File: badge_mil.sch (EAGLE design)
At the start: 29 parts, among them U1 TINY2313-*S*, X1 FH12-10S-0.5SH

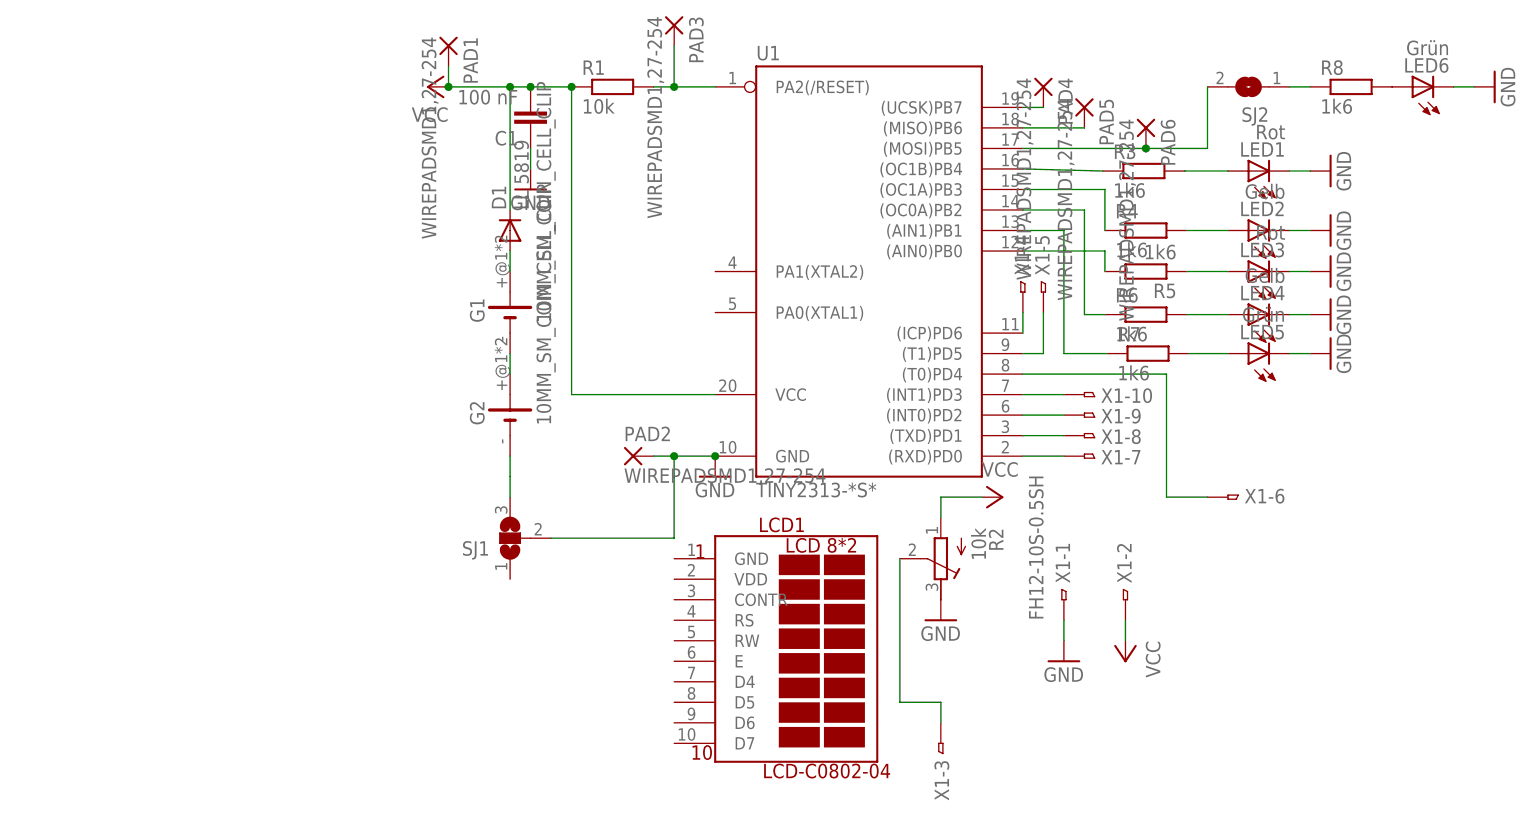
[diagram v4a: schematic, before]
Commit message: redesign, add render scripts
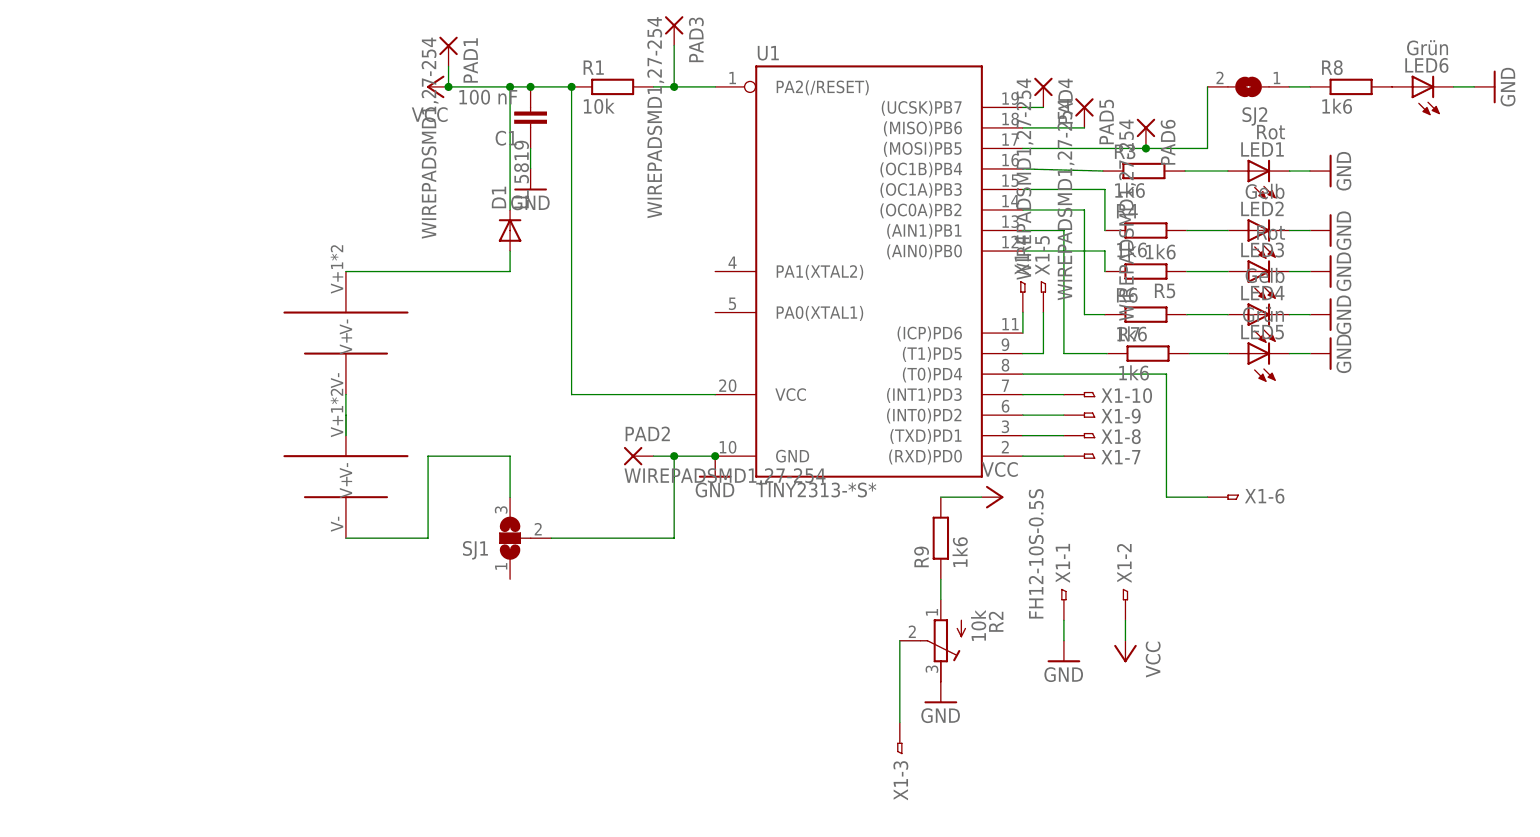
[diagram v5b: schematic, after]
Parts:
- removed G1, G2: 10MM_SM_COIN_CELL_CLIP, battery:10MM_SM_COIN_CELL_CLIP
- removed LCD1: LCD-C0802-04, lcd-c0802-04:LCD-C0802-04
- added R9: 1k6, resistor:R-EU_R0805
- added U$1, U$2: KEYSTONE3002, draradech:KEYSTONE3002
- X1: value FH12-10S-0.5SH -> FH12-10S-0.5S; device con-hirose:FH12-10S-0.5SH -> con-hirose:FH12-10S-0.5S
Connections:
- new net N$21: R2.E, R9.1
- net N$28: now also U$2.V-; no longer G2.-
- net N$37: now also U$1.V+; no longer G1.+
- net N$8: now also U$1.V-, U$2.V+; no longer G1.-, G2.+
- net VCC: now also R9.2; no longer R2.E
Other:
- moved on the sheet: R2, X1-3
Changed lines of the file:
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@@
 <?xml version="1.0" encoding="utf-8"?>
 <!DOCTYPE eagle SYSTEM "eagle.dtd">
-<eagle version="7.1.0">
+<eagle version="7.2.0">
 <drawing>
 <settings>
@@
 <setting verticaltext="up"/>
 </settings>
-<grid distance="0.1" unitdist="inch" unit="inch" style="lines" multiple="1" display="no" altdistance="0.01" altunitdist="inch" altunit="inch"/>
+<grid distance="100" unitdist="mil" unit="mil" style="lines" multiple="1" display="yes" altdistance="0.01" altunitdist="inch" altunit="inch"/>
 <layers>
 <layer number="1" name="Top" color="4" fill="1" visible="no" active="no"/>
@@
 <part name="P+1" library="supply1" deviceset="VCC" device=""/>
 <part name="GND2" library="supply1" deviceset="GND" device=""/>
-<part name="G2" library="battery" deviceset="10MM_SM_COIN_CELL_CLIP" device=""/>
 <part name="LED1" library="led" deviceset="LED" device="SML0603" value="Rot"/>
 <part name="LED6" library="led" deviceset="LED" device="SML0603" value="Grün"/>
@@
 <part name="R6" library="resistor" deviceset="R-EU_" device="R0805" value="1k6"/>
 <part name="R7" library="resistor" deviceset="R-EU_" device="R0805" value="1k6"/>
-<part name="X1" library="con-hirose" deviceset="FH12-10S-0.5S" device="H"/>
+<part name="X1" library="con-hirose" deviceset="FH12-10S-0.5S" device="" value="FH12-10S-0.5S"/>
 <part name="GND4" library="supply1" deviceset="GND" device=""/>
 <part name="P+3" library="supply1" deviceset="VCC" device=""/>
@@
 <part name="GND7" library="supply1" deviceset="GND" device=""/>
 <part name="R5" library="resistor" deviceset="R-EU_" device="R0805" value="1k6"/>
-<part name="G1" library="battery" deviceset="10MM_SM_COIN_CELL_CLIP" device=""/>
 <part name="D1" library="diode" deviceset="DIODE-" device="MELF-MLL41" value="LL 5819"/>
-<part name="LCD1" library="lcd-c0802-04" deviceset="LCD-C0802-04" device=""/>
 <part name="PAD1" library="wirepad" deviceset="WIREPAD" device="SMD1,27-254"/>
 <part name="PAD3" library="wirepad" deviceset="WIREPAD" device="SMD1,27-254"/>
@@
 <part name="R2" library="resistor" deviceset="R-TRIMM" device="4G/J" value="10k"/>
 <part name="GND3" library="supply1" deviceset="GND" device=""/>
+<part name="R9" library="resistor" deviceset="R-EU_" device="R0805" value="1k6"/>
+<part name="U$1" library="draradech" deviceset="KEYSTONE3002" device=""/>
+<part name="U$2" library="draradech" deviceset="KEYSTONE3002" device=""/>
 </parts>
 <sheets>
@@
 <instance part="P+1" gate="VCC" x="-22.86" y="66.04" rot="R90"/>
 <instance part="GND2" gate="1" x="12.7" y="17.78"/>
-<instance part="G2" gate="G$1" x="-12.7" y="25.4" rot="R90"/>
 <instance part="LED1" gate="G$1" x="78.74" y="55.626" rot="R90"/>
 <instance part="LED6" gate="G$1" x="99.06" y="66.04" rot="R90"/>
@@
 <instance part="X1" gate="-1" x="55.88" y="2.54" rot="R90"/>
 <instance part="X1" gate="-2" x="63.5" y="2.54" rot="R90"/>
-<instance part="X1" gate="-3" x="40.64" y="-15.24" rot="R270"/>
+<instance part="X1" gate="-3" x="35.56" y="-15.24" rot="R270"/>
 <instance part="X1" gate="-4" x="50.8" y="40.64" rot="R90"/>
 <instance part="X1" gate="-5" x="53.34" y="40.64" rot="R90"/>
@@
 <instance part="GND7" gate="1" x="88.9" y="43.18" rot="R90"/>
 <instance part="R5" gate="G$1" x="66.04" y="43.18" rot="R180"/>
-<instance part="G1" gate="G$1" x="-12.7" y="38.1" rot="R90"/>
 <instance part="D1" gate="G$1" x="-12.7" y="48.26" rot="R90"/>
-<instance part="LCD1" gate="G$1" x="20.32" y="-2.54"/>
 <instance part="PAD1" gate="G$1" x="-20.32" y="71.12" rot="R270"/>
 <instance part="PAD3" gate="G$1" x="7.62" y="73.66" rot="R270"/>
@@
 <instance part="SJ2" gate="1" x="78.74" y="66.04" rot="R180"/>
 <instance part="SJ1" gate="G$1" x="-12.7" y="10.16" rot="R180"/>
-<instance part="R2" gate="G$1" x="40.64" y="7.62" rot="R180"/>
-<instance part="GND3" gate="1" x="40.64" y="0"/>
+<instance part="R2" gate="G$1" x="40.64" y="-2.54" rot="R180"/>
+<instance part="GND3" gate="1" x="40.64" y="-10.16"/>
+<instance part="R9" gate="G$1" x="40.64" y="10.16" rot="R90"/>
+<instance part="U$1" gate="G$1" x="-33.02" y="35.56" rot="R180"/>
+<instance part="U$2" gate="G$1" x="-33.02" y="17.78" rot="R180"/>
 </instances>
 <busses>
@@
 </segment>
 <segment>
-<pinref part="P+2" gate="VCC" pin="VCC"/>
-<wire x1="45.72" y1="15.24" x2="40.64" y2="15.24" width="0.1524" layer="91"/>
-<wire x1="40.64" y1="15.24" x2="40.64" y2="12.7" width="0.1524" layer="91"/>
-<pinref part="R2" gate="G$1" pin="E"/>
-</segment>
-<segment>
 <pinref part="P+3" gate="VCC" pin="VCC"/>
 <pinref part="X1" gate="-2" pin="1"/>
 <wire x1="63.5" y1="-2.54" x2="63.5" y2="0" width="0.1524" layer="91"/>
+</segment>
+<segment>
+<pinref part="R9" gate="G$1" pin="2"/>
+<pinref part="P+2" gate="VCC" pin="VCC"/>
+<wire x1="40.64" y1="15.24" x2="45.72" y2="15.24" width="0.1524" layer="91"/>
 </segment>
 </net>
@@
 </segment>
 </net>
-<net name="N$8" class="0">
-<segment>
-<pinref part="G2" gate="G$1" pin="+"/>
-<pinref part="G1" gate="G$1" pin="-"/>
-<wire x1="-12.7" y1="30.48" x2="-12.7" y2="33.02" width="0.1524" layer="91"/>
-</segment>
-</net>
 <net name="N$37" class="0">
 <segment>
-<pinref part="G1" gate="G$1" pin="+"/>
 <pinref part="D1" gate="G$1" pin="A"/>
 <wire x1="-12.7" y1="43.18" x2="-12.7" y2="45.72" width="0.1524" layer="91"/>
+<pinref part="U$1" gate="G$1" pin="V+"/>
+<wire x1="-12.7" y1="43.18" x2="-33.02" y2="43.18" width="0.1524" layer="91"/>
 </segment>
 </net>
@@
 <net name="N$28" class="0">
 <segment>
-<pinref part="G2" gate="G$1" pin="-"/>
-<wire x1="-12.7" y1="17.78" x2="-12.7" y2="20.32" width="0.1524" layer="91"/>
 <pinref part="SJ1" gate="G$1" pin="3"/>
-<wire x1="-12.7" y1="15.24" x2="-12.7" y2="17.78" width="0.1524" layer="91"/>
+<wire x1="-12.7" y1="15.24" x2="-12.7" y2="20.32" width="0.1524" layer="91"/>
+<pinref part="U$2" gate="G$1" pin="V-"/>
+<wire x1="-33.02" y1="10.16" x2="-22.86" y2="10.16" width="0.1524" layer="91"/>
+<wire x1="-22.86" y1="10.16" x2="-22.86" y2="20.32" width="0.1524" layer="91"/>
+<wire x1="-22.86" y1="20.32" x2="-12.7" y2="20.32" width="0.1524" layer="91"/>
 </segment>
 </net>
@@
 <segment>
 <pinref part="X1" gate="-3" pin="1"/>
-<wire x1="40.64" y1="-10.16" x2="40.64" y2="-12.7" width="0.1524" layer="91"/>
 <pinref part="R2" gate="G$1" pin="S"/>
-<wire x1="35.56" y1="7.62" x2="35.56" y2="-10.16" width="0.1524" layer="91"/>
-<wire x1="35.56" y1="-10.16" x2="40.64" y2="-10.16" width="0.1524" layer="91"/>
-</segment>
-</net>
+<wire x1="35.56" y1="-2.54" x2="35.56" y2="-12.7" width="0.1524" layer="91"/>
+</segment>
+</net>
+<net name="N$21" class="0">
+<segment>
+<pinref part="R2" gate="G$1" pin="E"/>
+<pinref part="R9" gate="G$1" pin="1"/>
+<wire x1="40.64" y1="2.54" x2="40.64" y2="5.08" width="0.1524" layer="91"/>
+</segment>
+</net>
+<net name="N$8" class="0">
+<segment>
+<pinref part="U$1" gate="G$1" pin="V-"/>
+<pinref part="U$2" gate="G$1" pin="V+"/>
+<wire x1="-33.02" y1="27.94" x2="-33.02" y2="25.4" width="0.1524" layer="91"/>
+<wire x1="-33.02" y1="25.4" x2="-33.02" y2="22.86" width="0.1524" layer="91"/>
+</segment>
+</net>

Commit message: MIC5205 for power supply
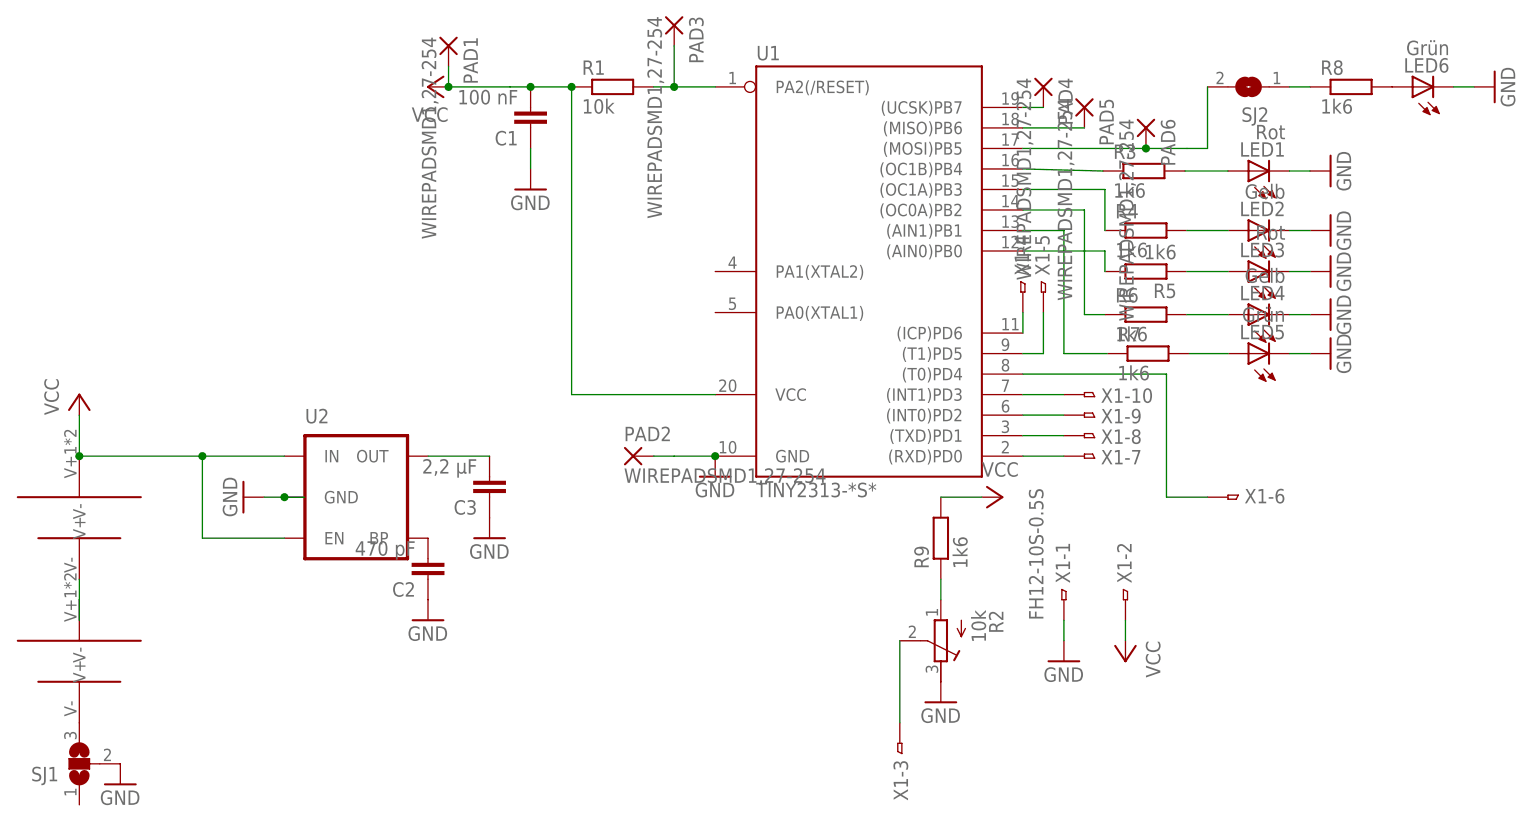
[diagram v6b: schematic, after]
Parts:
- removed D1: LL 5819, diode:DIODE-MELF-MLL41
- added C2: 470 pF, rcl:C-EUC0805
- added C3: 2,2 µF, rcl:C-EUC0805
- added U2: (no value), SparkFun-PowerIC:MIC52055V
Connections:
- new net N$28: C2.2, U2.BP
- net GND: now also C2.1, C3.1, U2.GND
- net N$37: now also C3.2, U2.OUT; no longer D1.A, U$1.V+
- net VCC: now also U$1.V+, U2.EN, U2.IN; no longer D1.C
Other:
- moved on the sheet: SJ1

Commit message: fix short circuit
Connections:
- removed net N$37: C3.2, U2.OUT
- new net N$29: U$1.V+, U2.EN, U2.IN
- net VCC: now also C3.2, U2.OUT; no longer U$1.V+, U2.EN, U2.IN
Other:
- moved on the sheet: LED1, LED3, LED5
